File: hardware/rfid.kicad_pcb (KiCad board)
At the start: 2 copper layers, 75 x 50 mm, 33 parts, among them P1 CONN_01X02, P2 COMMS, U1 CR95HF, X1 27.12MHz

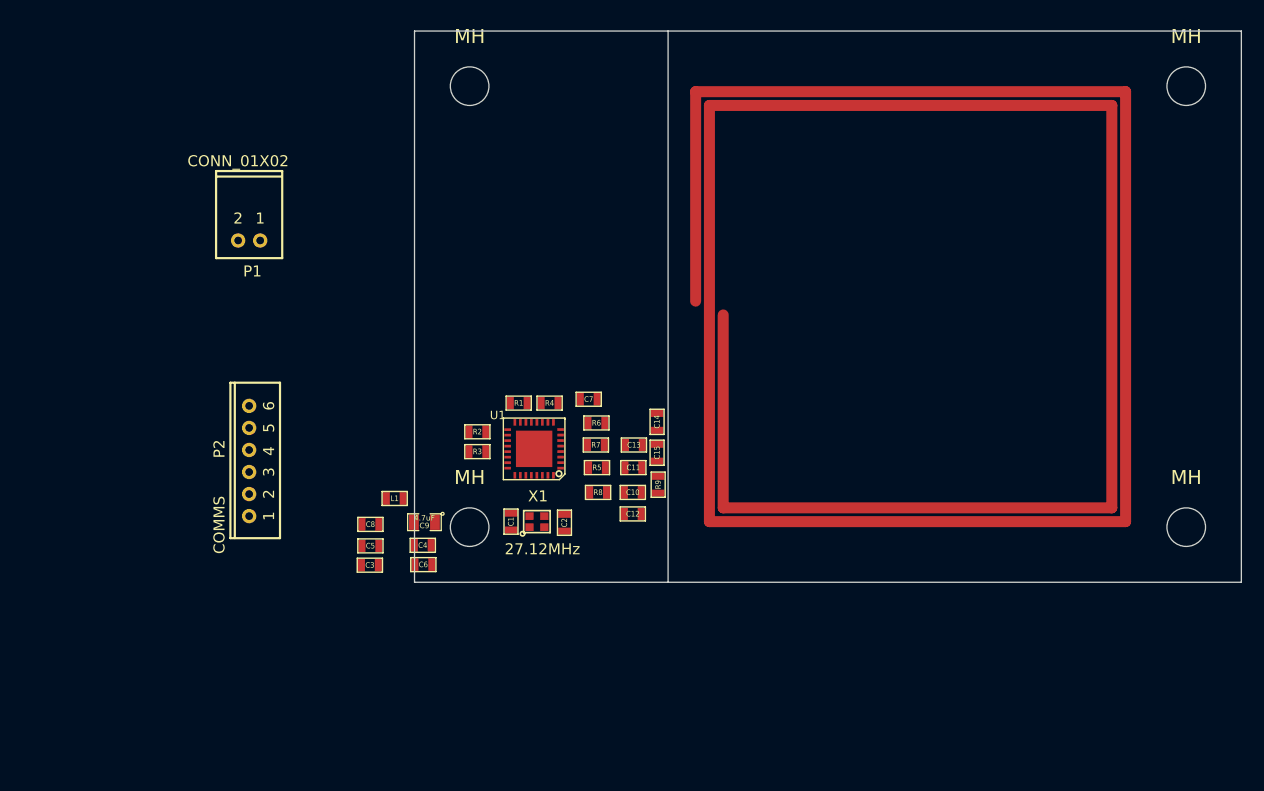
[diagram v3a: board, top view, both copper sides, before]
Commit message: Moved components to about where they should go and started routing some traces.
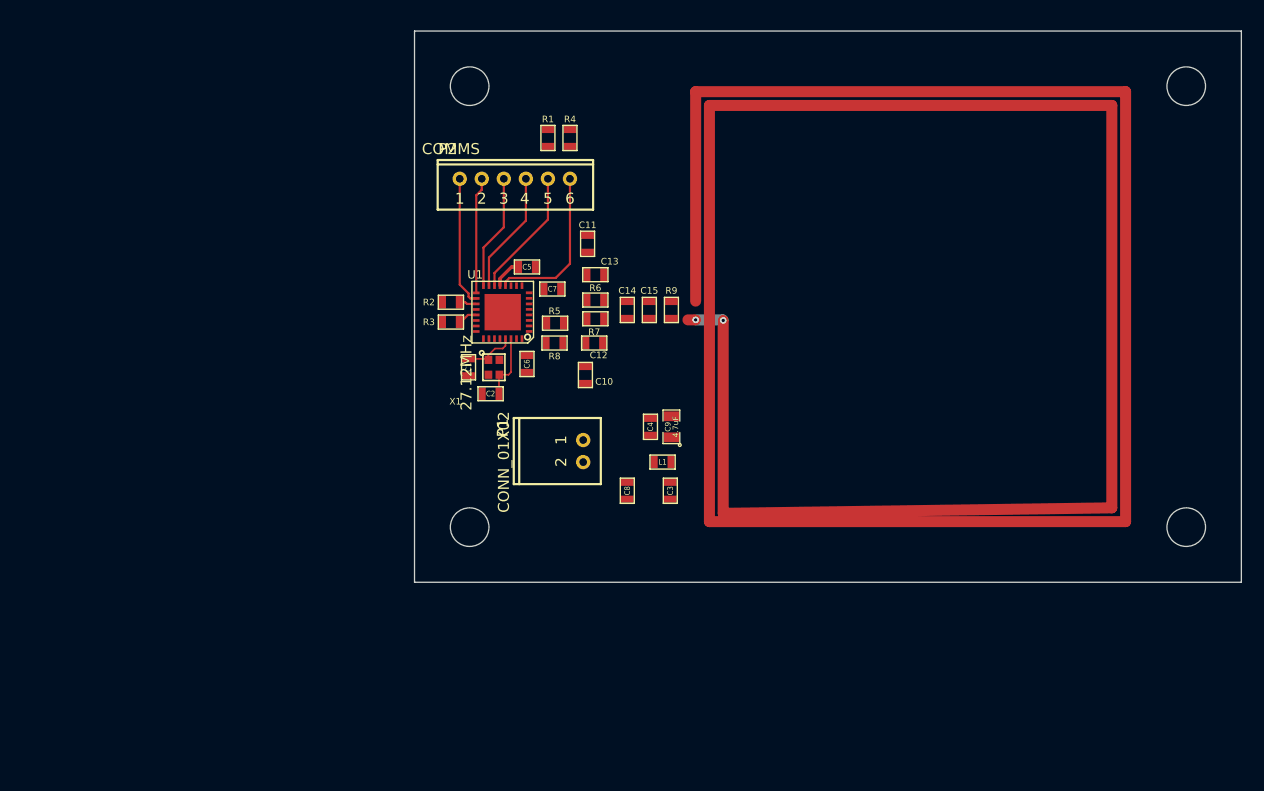
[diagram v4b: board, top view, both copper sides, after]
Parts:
- moved P2 35.2 mm to (164.1, 73.4), turned to 0 degrees
- moved P1 31.7 mm to (171.3, 95.1), turned to 90 degrees
- moved C5 29.0 mm to (166.2, 81.4), turned to 0 degrees
- moved C3 28.1 mm to (179.2, 101.7), turned to 270 degrees
- moved L1 24.5 mm to (178.5, 99.1)
- moved R1 24.2 mm to (168.1, 69.7), turned to 270 degrees
- moved R4 24.1 mm to (170.1, 69.7), turned to 270 degrees
- moved C9 24.0 mm to (179.3, 95.9), turned to 90 degrees
- moved C8 23.5 mm to (175.3, 101.7), turned to 270 degrees
- moved C4 23.3 mm to (177.4, 95.9), turned to 90 degrees
- moved C11 20.7 mm to (171.7, 79.3), turned to 270 degrees
- moved C6 20.5 mm to (166.2, 90.2), turned to 270 degrees
- moved R9 15.9 mm to (179.3, 85.3)
- moved C12 15.9 mm to (172.3, 88.3)
- moved C13 15.8 mm to (172.4, 82.1)
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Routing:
- net Net-(P2-Pad6): track 0.00 -> 14.6 mm
- net Net-(P2-Pad1): track 0.00 -> 11.8 mm
- net Net-(P2-Pad5): track 0.00 -> 11.7 mm
- net Net-(P2-Pad4): track 0.00 -> 11.1 mm
- net Net-(P2-Pad2): track 0.00 -> 10.6 mm
- net Net-(P2-Pad3): track 0.00 -> 10.5 mm
- net Net-(C2-Pad1): track 0.00 -> 5.93 mm
- net Net-(C1-Pad1): track 0.00 -> 4.81 mm
- net (no net): track 298.2 -> 301.5 mm, vias 0 -> 2
- net 3V3: track 0.00 -> 2.77 mm
- net Net-(R3-Pad1): track 0.00 -> 1.81 mm
- net Net-(R2-Pad1): track 0.00 -> 1.60 mm
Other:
- outline, holes or cut-outs redrawn

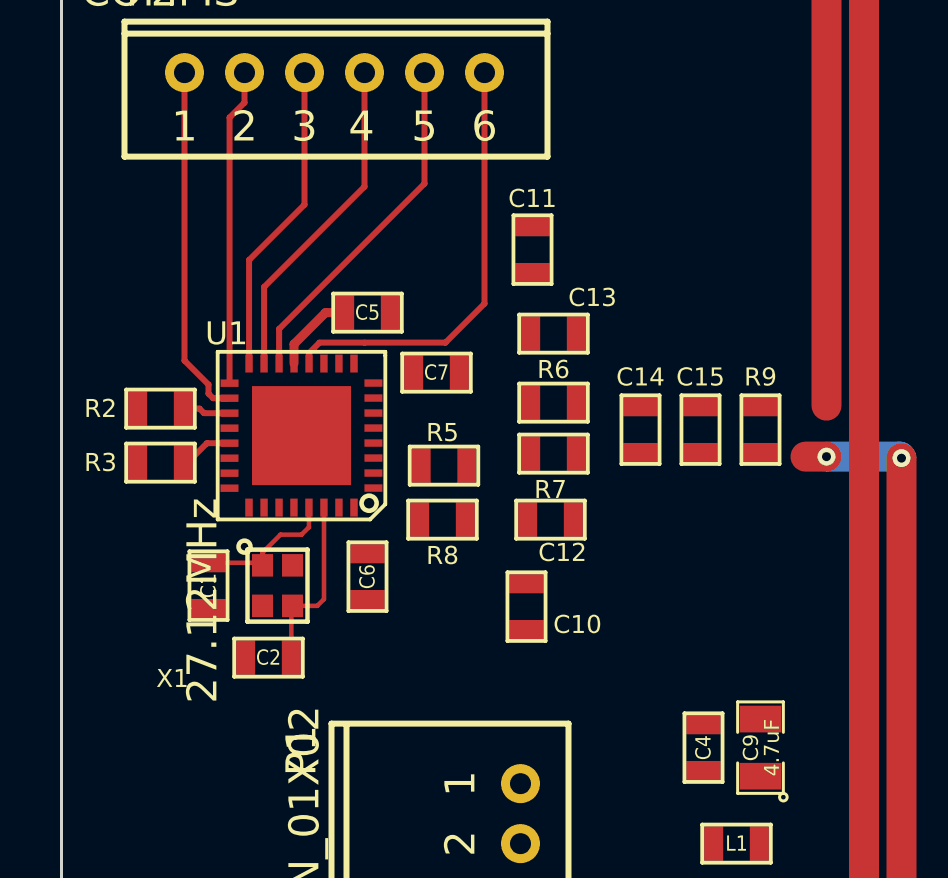
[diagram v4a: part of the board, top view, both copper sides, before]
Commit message: Shorted resistor attached to antenna in schematic like the antenna basically will (to prevent DRC errors). Also renamed the crystal from X1 to G1.
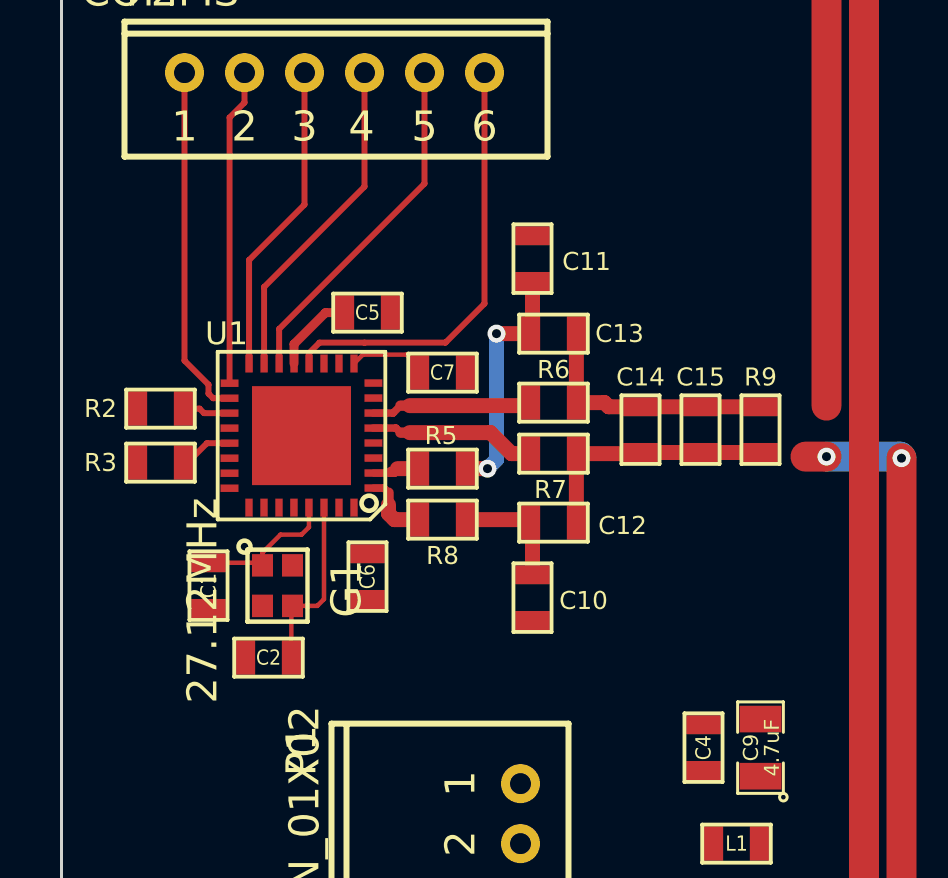
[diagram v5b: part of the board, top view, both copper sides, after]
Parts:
- removed X1: 27.12MHz, rfid:2x1.6_crystal
- added G1: 27.12MHz, rfid:2x1.6_crystal, F.Cu at (163.2, 90.5)
- moved C10 0.36 mm to (171.7, 90.9)
- moved C11 0.30 mm to (171.7, 79.6)
- moved C7 0.20 mm to (168.7, 83.4)
- moved C12 0.14 mm to (172.4, 88.4)
- moved R5 0.11 mm to (168.7, 86.6)
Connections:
- C13 pad 1: Net-(C13-Pad1) -> Net-(C12-Pad1)
- C14 pad 2: Net-(C13-Pad1) -> Net-(C12-Pad1)
- C15 pad 2: Net-(C13-Pad1) -> Net-(C12-Pad1)
- R6 pad 1: Net-(C13-Pad1) -> Net-(C12-Pad1)
- R9 pad 2: Net-(C13-Pad1) -> Net-(C12-Pad1)
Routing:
- net Net-(C12-Pad1): track 0.00 -> 16.9 mm
- net Net-(C11-Pad2): track 0.00 -> 8.26 mm, vias 0 -> 2
- net Net-(R7-Pad2): track 0.00 -> 5.59 mm
- net Net-(R6-Pad2): track 0.00 -> 5.38 mm
- net Net-(C10-Pad2): track 0.00 -> 3.98 mm
- net Net-(C7-Pad1): track 0.00 -> 2.65 mm
- net Net-(R8-Pad2): track 0.00 -> 2.39 mm
- net Net-(R5-Pad2): track 0.00 -> 1.60 mm

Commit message: Added flood fills for power stuff and connected antenna to RF passives.
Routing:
- net Net-(C12-Pad1): track 16.9 -> 321.3 mm, vias 0 -> 2
- net (no net): track 301.5 -> 0.00 mm, vias 2 -> 0
- net 3V3_RF: track 0.00 -> 17.5 mm
- added copper zone on F.Cu, net 3V3
- added copper zone on F.Cu, net 3V3_RF
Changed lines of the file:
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@@
   (general
     (links 61)
-    (no_connects 31)
-    (area 155.949999 59.949999 231.050001 110.050001)
+    (no_connects 24)
+    (area 135.37017 59.926 251.62983 111.37046)
     (thickness 1.6)
     (drawings 4)
-    (tracks 107)
+    (tracks 123)
     (zones 0)
     (modules 33)
@@
   )
   (setup
-    (last_trace_width 0.5)
+    (last_trace_width 1)
     (user_trace_width 0.15)
     (user_trace_width 0.2)
@@
     (user_trace_width 1)
     (trace_clearance 0.15)
-    (zone_clearance 0.508)
+    (zone_clearance 0.15)
     (zone_45_only no)
     (trace_min 0.15)
@@
     (pad_to_mask_clearance 0)
     (aux_axis_origin 0 0)
-    (visible_elements FFFEFFFF)
+    (visible_elements FFFEFF7F)
     (pcbplotparams
       (layerselection 0x00030_80000001)
@@
     (at 179.2 101.7 270)
     (attr smd)
-    (fp_text reference C3 (at 0 0 270) (layer F.SilkS)
-      (effects (font (size 0.508 0.4572) (thickness 0.1143)))
+    (fp_text reference C3 (at 1.8 0 360) (layer F.SilkS)
+      (effects (font (size 0.6 0.6) (thickness 0.15)))
     )
     (fp_text value 10nF (at 0 0 270) (layer F.SilkS) hide
@@
     (at 177.4 95.9 90)
     (attr smd)
-    (fp_text reference C4 (at 0 0 90) (layer F.SilkS)
-      (effects (font (size 0.508 0.4572) (thickness 0.1143)))
+    (fp_text reference C4 (at 1.7 0 180) (layer F.SilkS)
+      (effects (font (size 0.6 0.6) (thickness 0.15)))
     )
     (fp_text value 10nF (at 0 0 90) (layer F.SilkS) hide
@@
     (at 175.3 101.7 270)
     (attr smd)
-    (fp_text reference C8 (at 0 0 270) (layer F.SilkS)
-      (effects (font (size 0.508 0.4572) (thickness 0.1143)))
+    (fp_text reference C8 (at 1.8 0 360) (layer F.SilkS)
+      (effects (font (size 0.6 0.6) (thickness 0.15)))
     )
     (fp_text value 1uF (at 0 0 270) (layer F.SilkS) hide
@@
     (at 179.3 95.9 90)
     (attr smd)
-    (fp_text reference C9 (at 0 -0.3175 90) (layer F.SilkS)
-      (effects (font (size 0.50038 0.50038) (thickness 0.10922)))
+    (fp_text reference C9 (at 2 0 180) (layer F.SilkS)
+      (effects (font (size 0.6 0.6) (thickness 0.15)))
     )
     (fp_text value 4.7uF (at 0 0.381 90) (layer F.SilkS)
@@
     (at 178.5 99.1)
     (attr smd)
-    (fp_text reference L1 (at 0 0) (layer F.SilkS)
-      (effects (font (size 0.508 0.4572) (thickness 0.1143)))
+    (fp_text reference L1 (at -1.9 0.1) (layer F.SilkS)
+      (effects (font (size 0.6 0.6) (thickness 0.15)))
     )
     (fp_text value tx_3v3_choke (at 0 0) (layer F.SilkS) hide
@@
   (gr_line (start 231 60) (end 231 110) (angle 90) (layer Edge.Cuts) (width 0.1))
   (gr_line (start 156 60) (end 231 60) (angle 90) (layer Edge.Cuts) (width 0.1))
-  (via (at 184 86.25) (size 0.6) (layers F.Cu B.Cu) (net 0))
-  (segment (start 219.25 66.75) (end 219.25 103.25) (width 1) (layer F.Cu) (net 0))
-  (segment (start 219.25 103.25) (end 184 103.75) (width 1) (layer F.Cu) (net 0))
-  (segment (start 184 103.75) (end 184 86.25) (width 1) (layer F.Cu) (net 0))
-  (segment (start 182.75 66.75) (end 182.75 104.5) (width 1) (layer F.Cu) (net 0))
-  (segment (start 181.5 65.5) (end 220.5 65.5) (width 1) (layer F.Cu) (net 0))
-  (segment (start 220.5 65.5) (end 220.5 104.5) (width 1) (layer F.Cu) (net 0))
-  (segment (start 220.5 104.5) (end 182.75 104.5) (width 1) (layer F.Cu) (net 0))
-  (segment (start 181.5 84.5) (end 181.5 65.5) (width 1) (layer F.Cu) (net 0))
-  (segment (start 182.75 66.75) (end 219.25 66.75) (width 1) (layer F.Cu) (net 0))
-  (segment (start 181.5 86.2) (end 180.8 86.2) (width 1) (layer F.Cu) (net 0))
-  (via (at 181.5 86.2) (size 0.6) (layers F.Cu B.Cu) (net 0))
-  (segment (start 183.95 86.2) (end 181.5 86.2) (width 1) (layer B.Cu) (net 0))
-  (segment (start 184 86.25) (end 183.95 86.2) (width 1) (layer B.Cu) (net 0))
   (segment (start 160.9 89.738) (end 162.613 89.738) (width 0.15) (layer F.Cu) (net 1))
   (segment (start 162.613 89.738) (end 162.7 89.825) (width 0.15) (layer F.Cu) (net 1))
@@
   (segment (start 163.75108 82.44892) (end 163.75108 83.09716) (width 0.3) (layer F.Cu) (net 4))
   (segment (start 164.8 81.4) (end 163.75108 82.44892) (width 0.3) (layer F.Cu) (net 4))
+  (segment (start 176.3285 96.662) (end 173.4165 93.75) (width 0.5) (layer F.Cu) (net 5))
+  (segment (start 177.4 96.662) (end 176.3285 96.662) (width 0.5) (layer F.Cu) (net 5))
+  (segment (start 173.4165 93.75) (end 170 93.75) (width 0.5) (layer F.Cu) (net 5))
+  (segment (start 170 93.75) (end 169 92.75) (width 0.5) (layer F.Cu) (net 5))
+  (segment (start 169 92.75) (end 169 90) (width 0.5) (layer F.Cu) (net 5))
+  (segment (start 168.438 89.438) (end 166.2 89.438) (width 0.5) (layer F.Cu) (net 5))
+  (segment (start 169 90) (end 168.438 89.438) (width 0.5) (layer F.Cu) (net 5))
+  (segment (start 165.75006 88.07556) (end 166.2 88.5255) (width 0.25) (layer F.Cu) (net 5))
+  (segment (start 165.75006 87.9003) (end 165.75006 88.07556) (width 0.25) (layer F.Cu) (net 5))
+  (segment (start 166.2 88.5255) (end 166.2 89.438) (width 0.25) (layer F.Cu) (net 5))
   (segment (start 167.938 83.4) (end 167.938 83.238) (width 0.15) (layer F.Cu) (net 6))
   (segment (start 167.938 83.238) (end 167.5 82.8) (width 0.15) (layer F.Cu) (net 6))
@@
   (segment (start 171.7 80.362) (end 171.7 82.038) (width 0.5) (layer F.Cu) (net 8))
   (segment (start 171.7 82.038) (end 171.638 82.1) (width 0.5) (layer F.Cu) (net 8))
+  (segment (start 180.59799 84.538) (end 181.462 84.538) (width 1) (layer F.Cu) (net 9))
+  (segment (start 181.462 84.538) (end 181.5 84.5) (width 1) (layer F.Cu) (net 9))
+  (segment (start 179.3 84.538) (end 180.59799 84.538) (width 0.5) (layer F.Cu) (net 9))
+  (via (at 184 86.25) (size 0.6) (layers F.Cu B.Cu) (net 9))
+  (segment (start 219.25 66.75) (end 219.25 103.25) (width 1) (layer F.Cu) (net 9))
+  (segment (start 219.25 103.25) (end 184 103.25) (width 1) (layer F.Cu) (net 9))
+  (segment (start 184 103.25) (end 184 86.25) (width 1) (layer F.Cu) (net 9))
+  (segment (start 182.75 66.75) (end 182.75 104.5) (width 1) (layer F.Cu) (net 9))
+  (segment (start 181.5 65.5) (end 220.5 65.5) (width 1) (layer F.Cu) (net 9))
+  (segment (start 220.5 65.5) (end 220.5 104.5) (width 1) (layer F.Cu) (net 9))
+  (segment (start 220.5 104.5) (end 182.75 104.5) (width 1) (layer F.Cu) (net 9))
+  (segment (start 182.75 66.75) (end 219.25 66.75) (width 1) (layer F.Cu) (net 9))
+  (segment (start 181.5 86.2) (end 180.8 86.2) (width 1) (layer F.Cu) (net 9))
+  (via (at 181.5 86.2) (size 0.6) (layers F.Cu B.Cu) (net 9))
+  (segment (start 183.95 86.2) (end 181.5 86.2) (width 1) (layer B.Cu) (net 9))
+  (segment (start 184 86.25) (end 183.95 86.2) (width 1) (layer B.Cu) (net 9))
   (segment (start 173.162 86.1) (end 173.162 88.4) (width 0.5) (layer F.Cu) (net 9))
   (segment (start 173.162 86.1) (end 175.262 86.1) (width 0.5) (layer F.Cu) (net 9))
@@
   (segment (start 175.3 84.538) (end 177.3 84.538) (width 0.5) (layer F.Cu) (net 9))
   (segment (start 177.3 84.538) (end 179.3 84.538) (width 0.5) (layer F.Cu) (net 9))
+  (segment (start 179.89 86.12) (end 180.42 86.12) (width 0.5) (layer F.Cu) (net 9))
+  (segment (start 179.832 86.062) (end 179.89 86.12) (width 0.5) (layer F.Cu) (net 9))
+  (segment (start 179.3 86.062) (end 179.832 86.062) (width 0.5) (layer F.Cu) (net 9))
+  (segment (start 181.5 84.5) (end 181.5 65.5) (width 1) (layer F.Cu) (net 9))
   (segment (start 162.25248 83.09716) (end 162.25248 79.64752) (width 0.2) (layer F.Cu) (net 10))
   (segment (start 164.1 77.8) (end 164.1 73.4) (width 0.2) (layer F.Cu) (net 10))
@@
   (segment (start 167.1 88.3) (end 167.938 88.3) (width 0.5) (layer F.Cu) (net 21))
   (segment (start 166.9 88.1) (end 167.1 88.3) (width 0.5) (layer F.Cu) (net 21))
+  (zone (net 4) (net_name 3V3) (layer F.Cu) (hatch full 0.508)
+    (connect_pads (clearance 0.15))
+    (min_thickness 0.15)
+    (fill yes (arc_segments 16) (thermal_gap 0.15) (thermal_bridge_width 0.5))
+    (polygon
+      (pts
+        (xy 180.2 101.4) (xy 170.3 101.4) (xy 170.3 98.2) (xy 178.2 98.2) (xy 178.2 100.2)
+        (xy 180.2 100.2)
+      )
+    )
+  )
+  (zone (net 5) (net_name 3V3_RF) (layer F.Cu) (hatch full 0.508)
+    (connect_pads (clearance 0.15))
+    (min_thickness 0.15)
+    (fill yes (arc_segments 16) (thermal_gap 0.15) (thermal_bridge_width 0.5))
+    (polygon
+      (pts
+        (xy 178.9 99.8) (xy 180.2 99.8) (xy 180.2 96.3) (xy 176.7 96.3) (xy 176.7 97.8)
+        (xy 178.9 97.8)
+      )
+    )
+  )
 )

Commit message: Routed everything except for grounds.
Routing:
- net 3V3: track 2.77 -> 66.3 mm, vias 0 -> 2
- net GND: track 0.00 -> 13.5 mm, vias 0 -> 4
- net Net-(P2-Pad5): track 11.7 -> 14.6 mm
- net Net-(P2-Pad6): track 14.6 -> 17.5 mm
